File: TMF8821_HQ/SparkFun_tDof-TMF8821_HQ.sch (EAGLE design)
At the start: 24 parts, among them J4 QWIIC_RIGHT_ANGLE, J5 QWIIC_RIGHT_ANGLE

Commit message: Adds default address to HQ boards, fixes some clearance issues
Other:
- note added: "Default Address: 0x41"
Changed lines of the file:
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@@
 <text x="58.42" y="165.1" size="1.778" layer="97" font="vector">VCC Range: 2.7V - 3.3V
 I/O VCC Range: 1.62V - 3.3V</text>
+<text x="83.82" y="111.76" size="1.778" layer="97" font="vector">Default Address: 0x41</text>
 </plain>
 <instances>

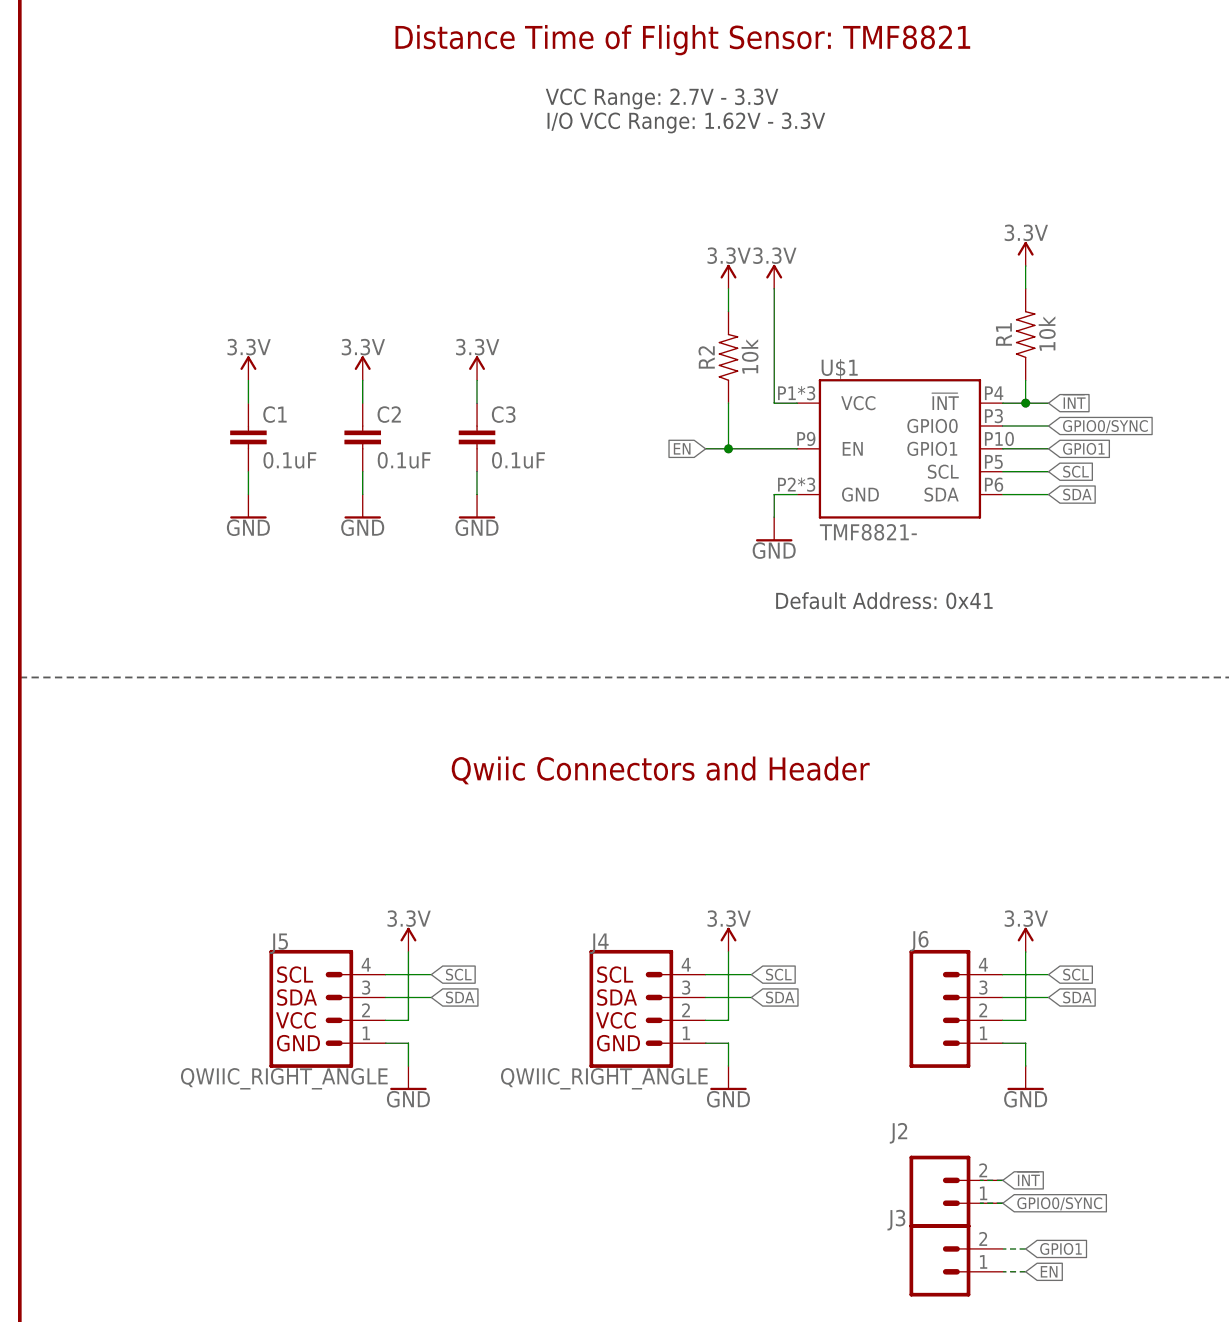
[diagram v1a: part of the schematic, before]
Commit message: Copies 8820 designs to create 8821 designs - updates relevant references to 8820 to 8821
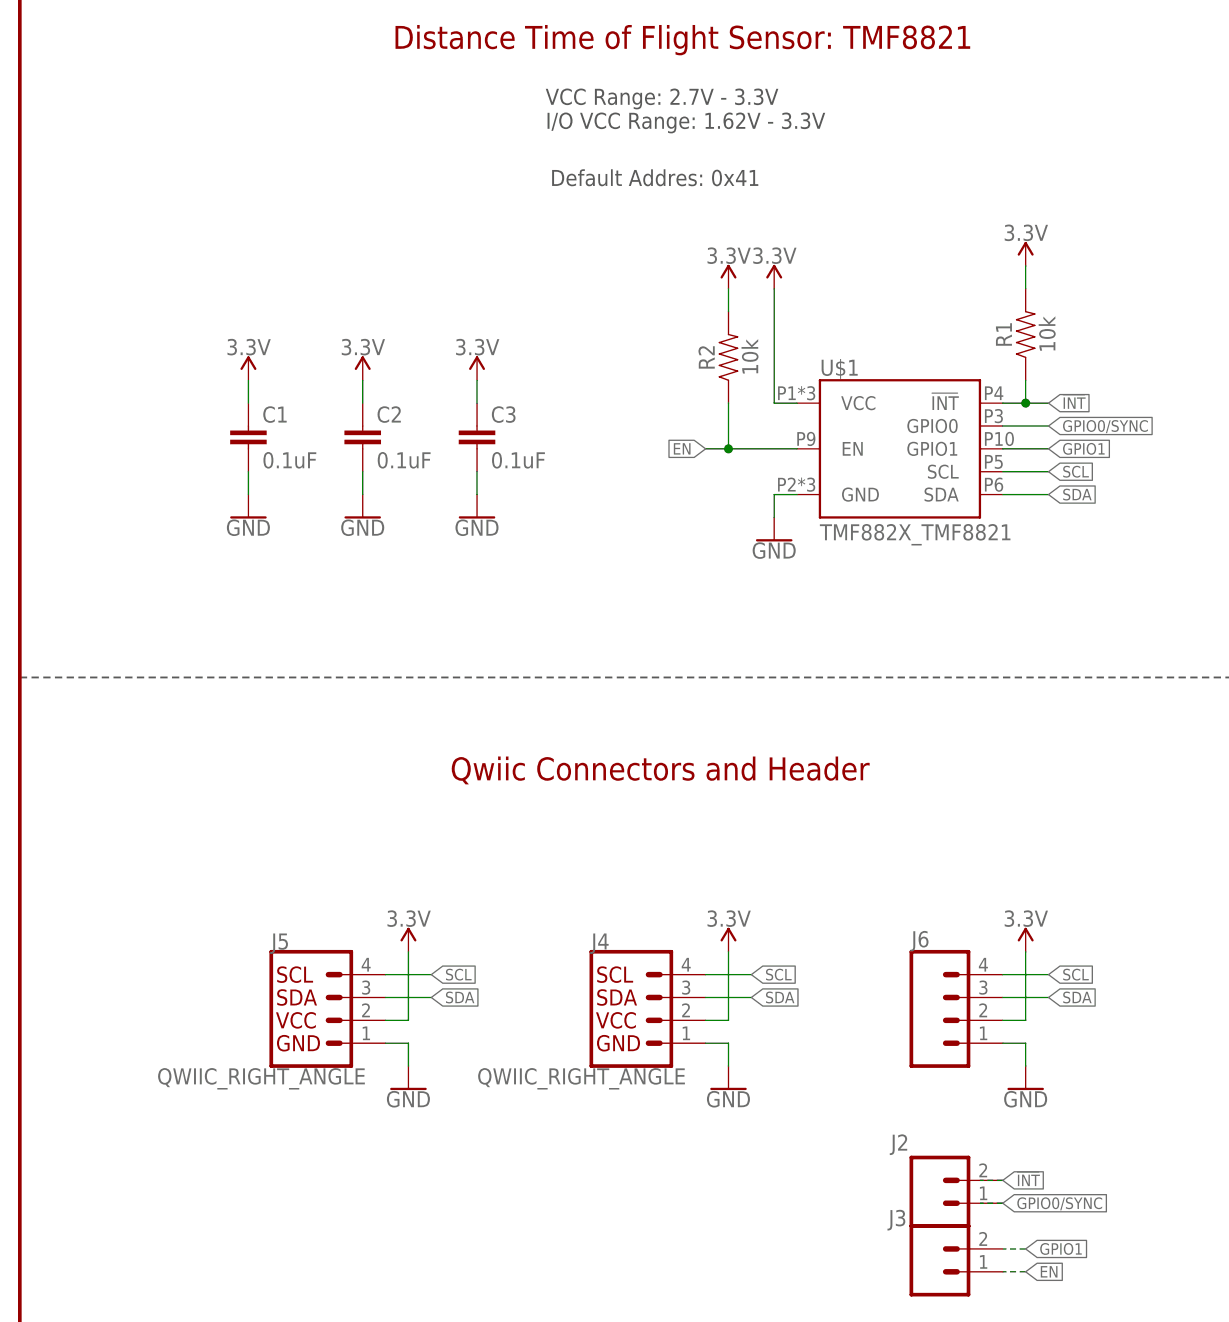
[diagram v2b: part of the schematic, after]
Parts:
- U$1: value TMF8821- -> TMF882X_TMF8821; device TMF882X:TMF8821- -> TMF882X:TMF882X_TMF8821
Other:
- note added: "Default Addres: 0x41"
- note removed: "Default Address: 0x41"
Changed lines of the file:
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@@
 <part name="I2C" library="SparkFun-Jumpers" deviceset="JUMPER-SMT_3_2-NC_TRACE" device="_SILK" package3d_urn="urn:adsk.eagle:package:39289/1" value="I2C_PU"/>
 <part name="SUPPLY10" library="SparkFun-PowerSymbols" deviceset="3.3V" device=""/>
-<part name="U$1" library="TMF882X" deviceset="TMF8821" device="-"/>
+<part name="U$1" library="TMF882X" deviceset="TMF882X" device="_TMF8821" value="TMF882X_TMF8821"/>
 <part name="C1" library="SparkFun-Capacitors" deviceset="0.1UF" device="-0402T-6.3V-10%-X7R" value="0.1uF"/>
 <part name="C2" library="SparkFun-Capacitors" deviceset="0.1UF" device="-0402T-6.3V-10%-X7R" value="0.1uF"/>
@@
 <text x="58.42" y="165.1" size="1.778" layer="97" font="vector">VCC Range: 2.7V - 3.3V
 I/O VCC Range: 1.62V - 3.3V</text>
-<text x="83.82" y="111.76" size="1.778" layer="97" font="vector">Default Address: 0x41</text>
+<text x="58.928" y="158.75" size="1.778" layer="97" font="vector">Default Addres: 0x41</text>
 </plain>
 <instances>
@@
 <instance part="H8" gate="G$1" x="236.22" y="27.94" smashed="yes"/>
 <instance part="J4" gate="G$1" x="68.58" y="66.04" smashed="yes">
-<attribute name="VALUE" x="53.34" y="60.706" size="1.778" layer="96" font="vector" align="top-left"/>
+<attribute name="VALUE" x="50.8" y="60.706" size="1.778" layer="96" font="vector" align="top-left"/>
 <attribute name="NAME" x="63.5" y="73.914" size="1.778" layer="95" font="vector"/>
 </instance>
 <instance part="J5" gate="G$1" x="33.02" y="66.04" smashed="yes">
-<attribute name="VALUE" x="17.78" y="60.706" size="1.778" layer="96" font="vector" align="top-left"/>
+<attribute name="VALUE" x="15.24" y="60.706" size="1.778" layer="96" font="vector" align="top-left"/>
 <attribute name="NAME" x="27.94" y="73.914" size="1.778" layer="95" font="vector"/>
 </instance>
@@
 <instance part="J2" gate="G$1" x="101.6" y="45.72" smashed="yes">
 <attribute name="VALUE" x="99.06" y="40.894" size="1.778" layer="96" font="vector"/>
-<attribute name="NAME" x="96.774" y="52.832" size="1.778" layer="95" font="vector"/>
+<attribute name="NAME" x="96.774" y="51.562" size="1.778" layer="95" font="vector"/>
 </instance>
 <instance part="J3" gate="G$1" x="101.6" y="38.1" smashed="yes">

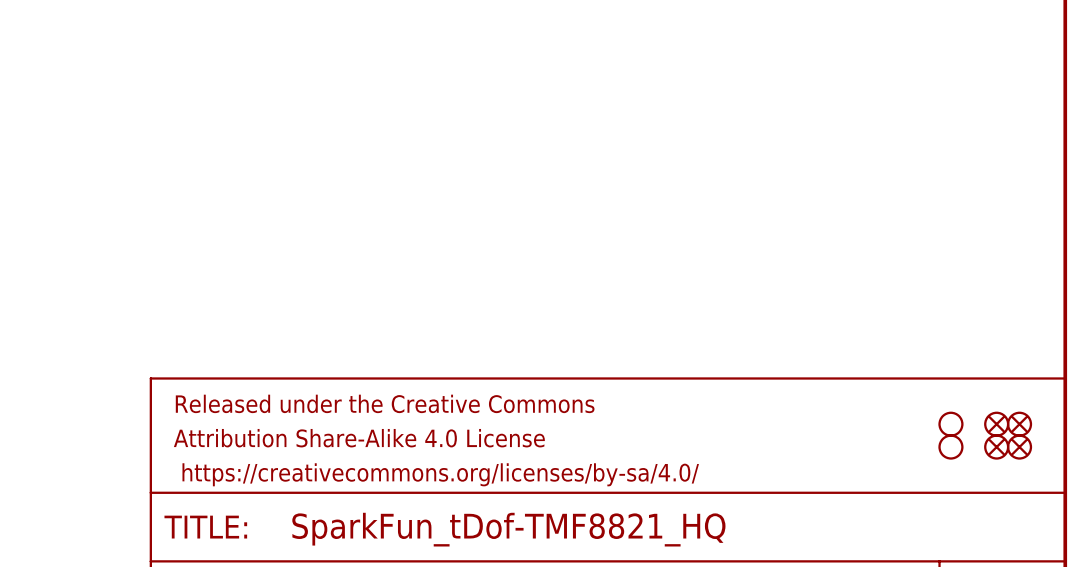
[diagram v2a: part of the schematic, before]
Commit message: Adds logos to schematic
* Moves measures to board (weren't moved when the design was put at the origin)
* Replaces IO1 silk with IO0 on GPIO0 PTH header
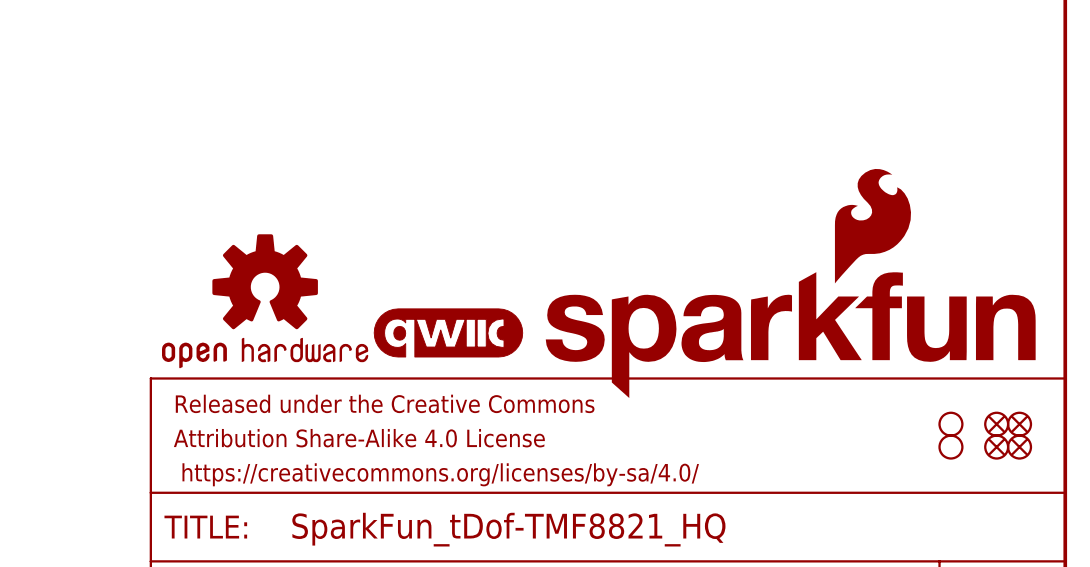
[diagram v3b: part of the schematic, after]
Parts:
- added LOGO1: SFE_LOGO_NAME_FLAMEBLANK, SparkFun-Aesthetics:SFE_LOGO_NAME_FLAMEBLANK
- added LOGO2: QWIIC_LOGO_3MM, SparkFun-Aesthetics:QWIIC_LOGO_3MM
- added LOGO3: OSHW-LOGONO_SILK, SparkFun-Aesthetics:OSHW-LOGONO_SILK
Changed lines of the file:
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@@
 <part name="J2" library="SparkFun-Connectors" deviceset="CONN_02" device="1X02_NO_SILK"/>
 <part name="J3" library="SparkFun-Connectors" deviceset="CONN_02" device="1X02_NO_SILK"/>
+<part name="LOGO1" library="SparkFun-Aesthetics" deviceset="SFE_LOGO_NAME_FLAME" device="BLANK"/>
+<part name="LOGO2" library="SparkFun-Aesthetics" deviceset="QWIIC_LOGO" device="_3MM"/>
+<part name="LOGO3" library="SparkFun-Aesthetics" deviceset="OSHW-LOGO" device="NO_SILK"/>
 </parts>
 <sheets>
@@
 <attribute name="NAME" x="96.52" y="43.18" size="1.778" layer="95" font="vector"/>
 </instance>
+<instance part="LOGO1" gate="G$1" x="190.5" y="33.02" smashed="yes"/>
+<instance part="LOGO2" gate="G$1" x="180.34" y="40.64" smashed="yes"/>
+<instance part="LOGO3" gate="G$1" x="160.02" y="45.72" smashed="yes"/>
 </instances>
 <busses>
